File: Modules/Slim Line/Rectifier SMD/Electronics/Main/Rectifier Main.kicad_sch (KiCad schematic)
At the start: 33 parts, among them J1 Negative HW, J2 Full Wave, J3 In, J4 Positive HW, J5 Power, U1 TL084CDT, U2 TL082CDT

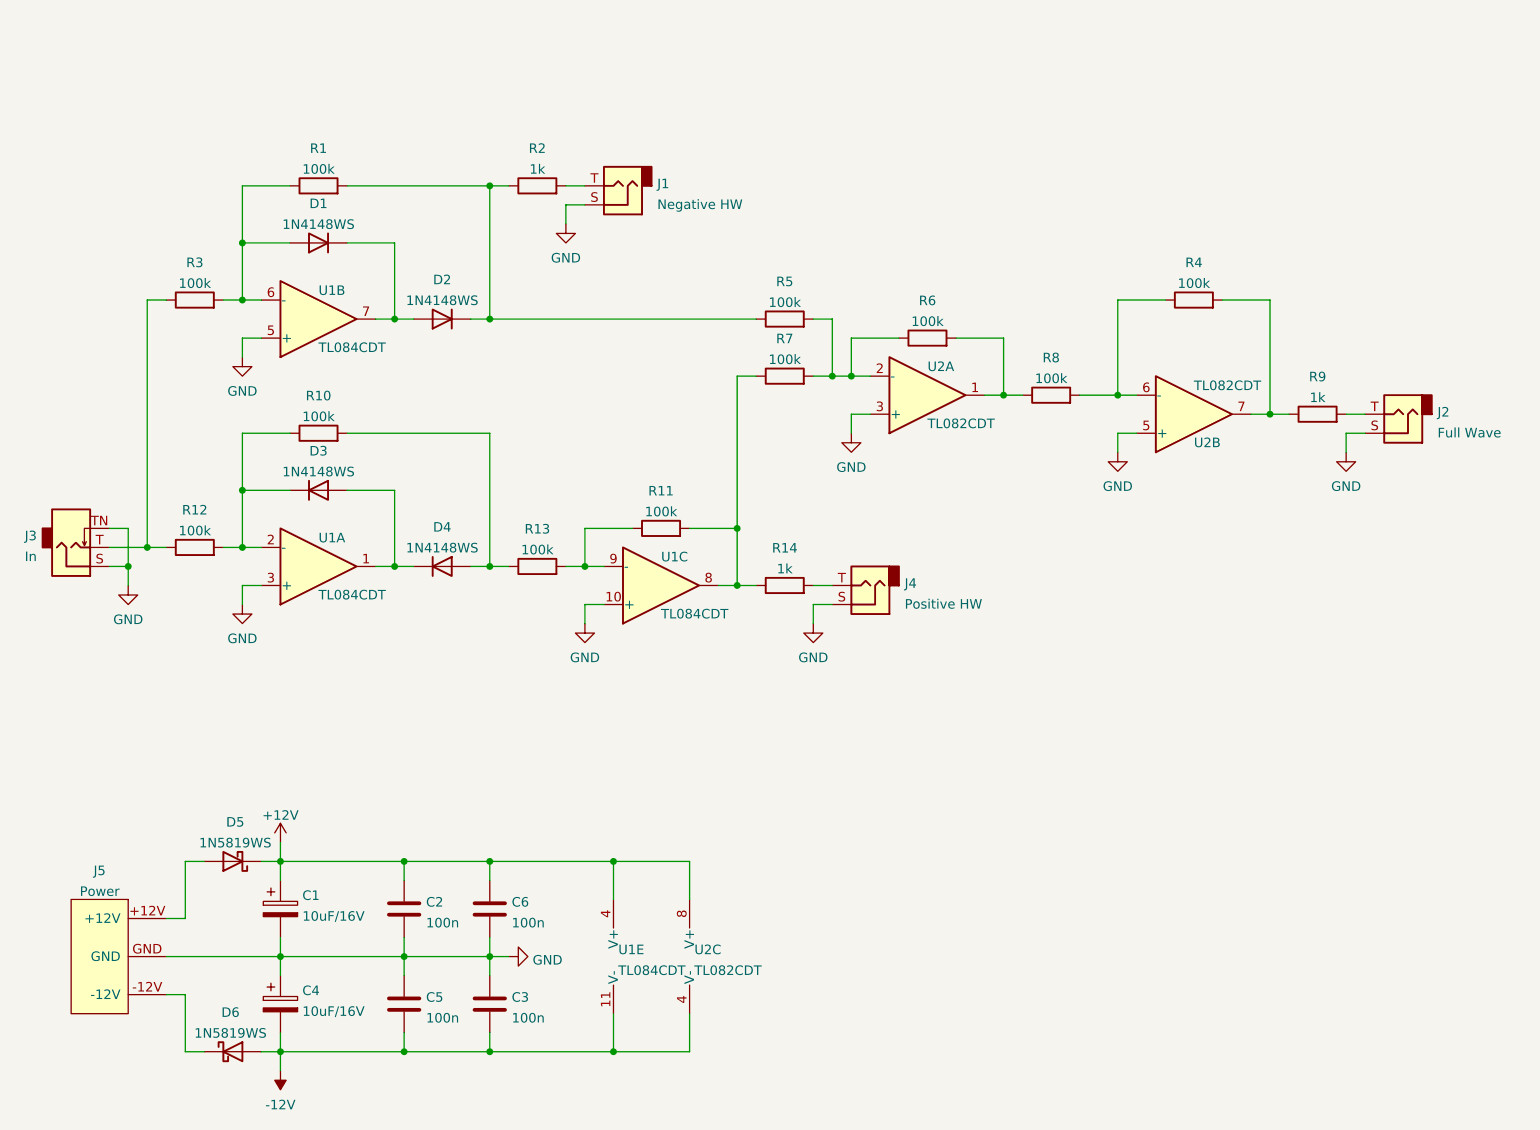
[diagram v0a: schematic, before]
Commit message: Update Sync LFO
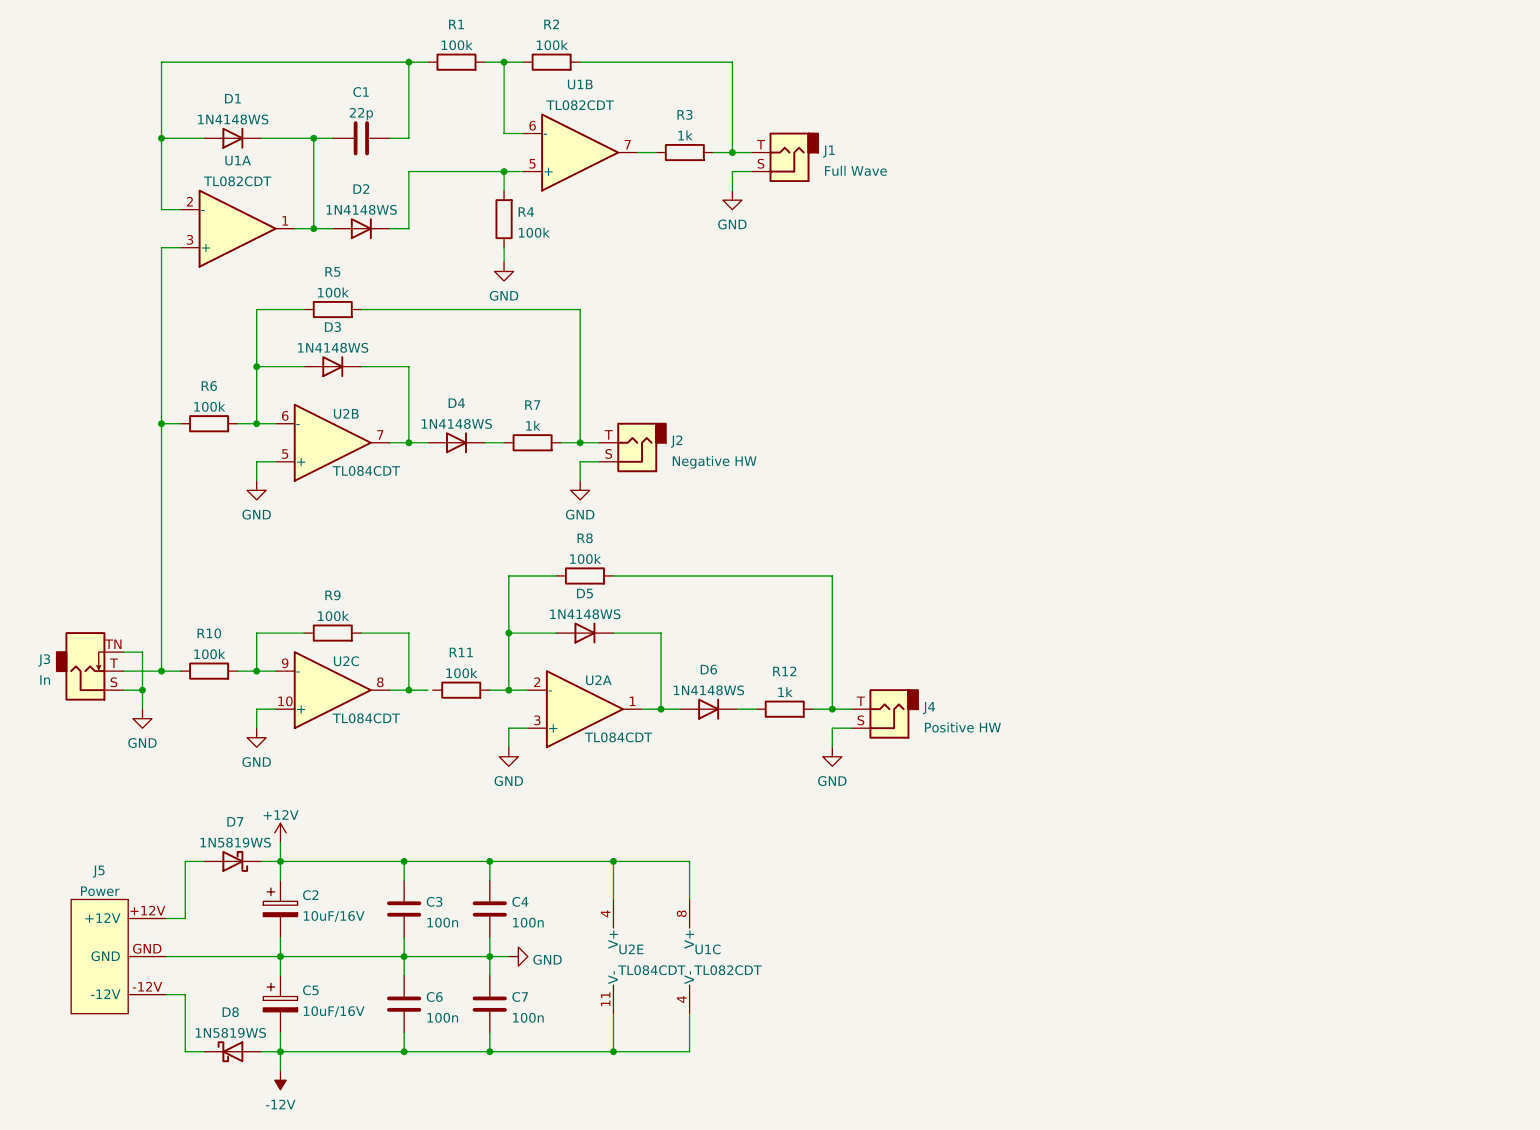
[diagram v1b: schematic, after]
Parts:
- removed R5, R6, R7, R8: 100k, Resistor_SMD:R_0402_1005Metric, symbol Device:R
- removed R9: 1k, Resistor_SMD:R_1206_3216Metric, symbol Device:R
- removed unit 2 of U2
- removed unit 1 of U2
- added C1: 22p, Capacitor_SMD:C_0402_1005Metric, symbol Device:C
- added D1, D2: 1N4148WS, Diode_SMD:D_SOD-323, symbol Diode:1N4148
- added R1, R2: 100k, Resistor_SMD:R_0603_1608Metric, symbol Device:R
- added R3: 1k, Resistor_SMD:R_1206_3216Metric, symbol Device:R
- added unit 2 of U1
- added unit 1 of U1
- C2: renamed from C1; footprint Capacitor_THT:CP_Radial_D5.0mm_P2.00mm -> Capacitor_Tantalum_SMD:CP_EIA-3216-18_Kemet-A; MPN (none) -> C7171
- C5: renamed from C4; footprint Capacitor_THT:CP_Radial_D5.0mm_P2.00mm -> Capacitor_Tantalum_SMD:CP_EIA-3216-18_Kemet-A; MPN (none) -> C7171
- D7: renamed from D5; footprint Diode_THT:D_DO-41_SOD81_P10.16mm_Horizontal -> Diode_SMD:D_SOD-323
- D8: renamed from D6; footprint Diode_THT:D_DO-41_SOD81_P10.16mm_Horizontal -> Diode_SMD:D_SOD-323
- R10: renamed from R13; footprint Resistor_SMD:R_0402_1005Metric -> Resistor_SMD:R_0603_1608Metric; MPN C25741 -> C335088
- R11: renamed from R12; footprint Resistor_SMD:R_0402_1005Metric -> Resistor_SMD:R_0603_1608Metric; MPN C25741 -> C335088
- R4: footprint Resistor_SMD:R_0402_1005Metric -> Resistor_SMD:R_0603_1608Metric; MPN C25741 -> C335088
- R5: renamed from R1; footprint Resistor_SMD:R_0402_1005Metric -> Resistor_SMD:R_0603_1608Metric; MPN C25741 -> C335088
- R6: renamed from R3; footprint Resistor_SMD:R_0402_1005Metric -> Resistor_SMD:R_0603_1608Metric; MPN C25741 -> C335088
- R8: renamed from R10; footprint Resistor_SMD:R_0402_1005Metric -> Resistor_SMD:R_0603_1608Metric; MPN C25741 -> C335088
- R9: renamed from R11; footprint Resistor_SMD:R_0402_1005Metric -> Resistor_SMD:R_0603_1608Metric; MPN C25741 -> C335088
- renumbered C2 to C3, C6 to C4, C5 to C6, C3 to C7, D1 to D3, D2 to D4, D3 to D5, D4 to D6, J2 to J1, J1 to J2, R14 to R12, R2 to R7, U2 to U1, U1 to U2
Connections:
- net GND: now also R4.1
- net at R11.2, R8.1, U2.2 (-): now also D5.2 (A); no longer D5.1 (K)
- net at R4.2: now also D2.1 (K), U1.5 (+)
- net at J1.T: now also R2.2, R3.2
- net at D4.1 (K), R7.1: no longer R5.2
- net at J2.T, R7.2: now also R5.2
- net at R9.2, U2.8: no longer R12.1
- net at J3.T, R6.1: now also R10.1, U1.3 (+); no longer R11.1
- net at J4.T, R12.2: now also R8.2
- new net: R1.2, R2.1, U1.6 (-)
- new net: R3.1, U1.7
- new net: C1.1, D1.2 (A), R1.1, U1.2 (-)
- new net: D5.1 (K), D6.2 (A), U2.1
- new net: C1.2, D1.1 (K), D2.2 (A), U1.1
- new net: D6.1 (K), R12.1
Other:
- moved on the sheet: D3, D4, D5, D6, J1, J2, J3, J4, R10, R11, R12, R5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

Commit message: Update
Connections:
- net at R9.2, U2.8: now also R11.1
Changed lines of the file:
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@@
     (stroke (width 0) (type default) (color 0 0 0 0))
   )
-  (wire (pts (xy 75.565 102.87) (xy 78.105 102.87))
+  (wire (pts (xy 75.565 102.87) (xy 78.74 102.87))
     (stroke (width 0) (type default) (color 0 0 0 0))
   )
